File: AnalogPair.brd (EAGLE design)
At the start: 61 x 100.3 mm, 45 parts, among them J1 POWERPOLE_POWER25A, Q1 35A/25V/8.5mΩ, Q10 35A/25V/8.5mΩ, Q2 35A/25V/8.5mΩ, Q3 35A/25V/8.5mΩ, Q4 35A/25V/8.5mΩ, Q5 35A/25V/8.5mΩ, Q6 35A/25V/8.5mΩ, Q7 35A/25V/8.5mΩ, Q8 35A/25V/8.5mΩ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

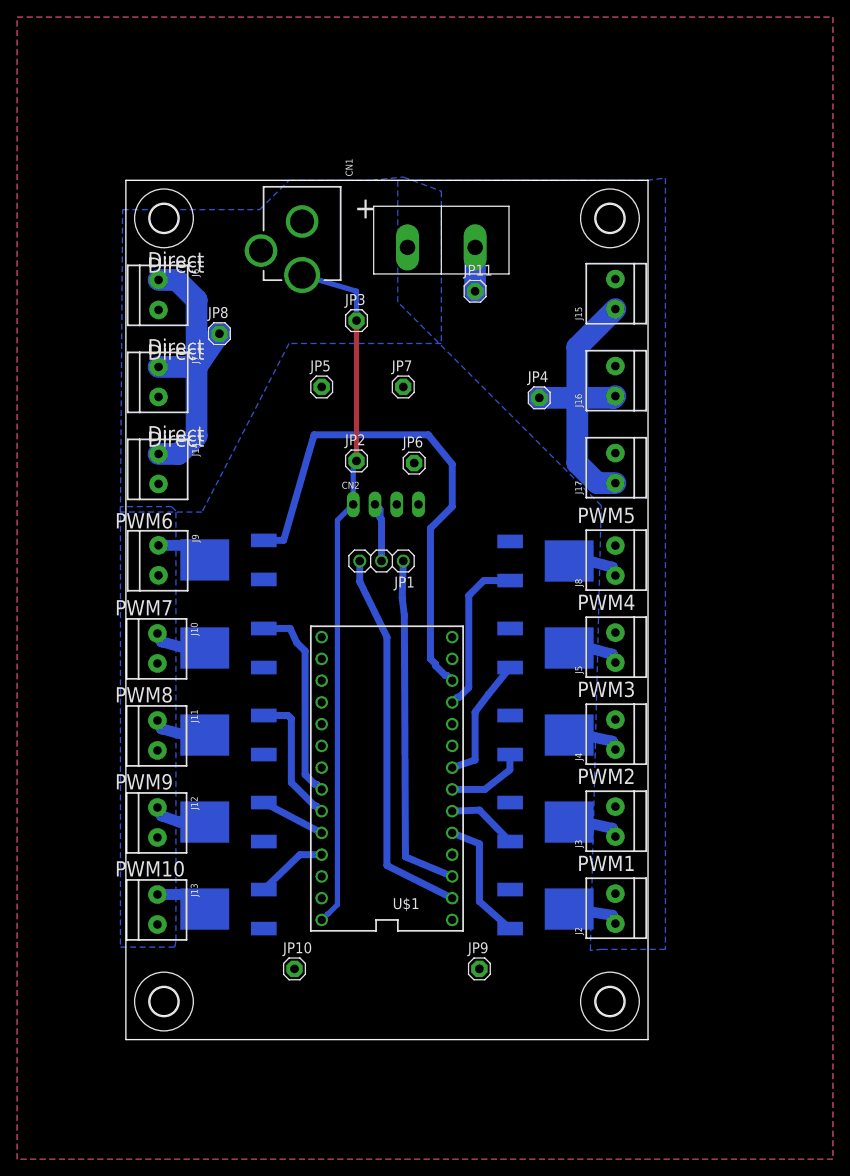
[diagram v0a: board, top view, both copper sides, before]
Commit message: added silks and submitted analogpair to allpcb.com
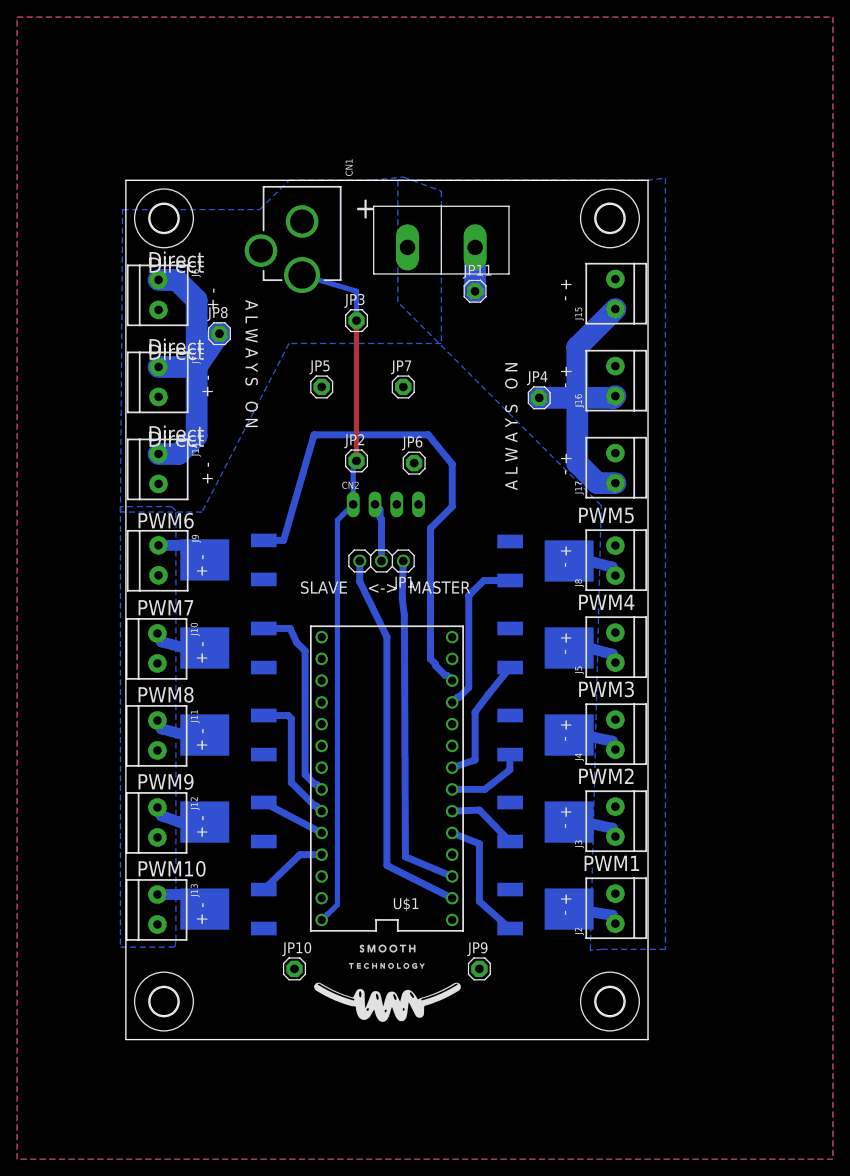
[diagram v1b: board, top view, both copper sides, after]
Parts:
- added U$13: (no value), SmoothTechnology:SMOOTH_
- added U$14: (no value), SmoothTechnology:TECHNOLOGY_
- added U$17: (no value), SmoothTechnology:SMOOTH_LOGO
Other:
- board text added: "+ -"
- board text added: "<->"
- board text added: "A L W A Y S O N"
- board text added: "MASTER"
- board text added: "SLAVE"
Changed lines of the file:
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@@
 <?xml version="1.0" encoding="utf-8"?>
 <!DOCTYPE eagle SYSTEM "eagle.dtd">
-<eagle version="8.5.2">
+<eagle version="8.6.0">
 <drawing>
 <settings>
-<setting alwaysvectorfont="no"/>
+<setting alwaysvectorfont="yes"/>
 <setting keepoldvectorfont="yes"/>
 <setting verticaltext="up"/>
@@
 <layer number="17" name="Pads" color="2" fill="1" visible="yes" active="yes"/>
 <layer number="18" name="Vias" color="2" fill="1" visible="yes" active="yes"/>
-<layer number="19" name="Unrouted" color="6" fill="1" visible="yes" active="yes"/>
-<layer number="20" name="Dimension" color="24" fill="1" visible="yes" active="yes"/>
+<layer number="19" name="Unrouted" color="6" fill="1" visible="no" active="yes"/>
+<layer number="20" name="Dimension" color="24" fill="1" visible="no" active="yes"/>
 <layer number="21" name="tPlace" color="7" fill="1" visible="yes" active="yes"/>
-<layer number="22" name="bPlace" color="7" fill="1" visible="yes" active="yes"/>
+<layer number="22" name="bPlace" color="7" fill="1" visible="no" active="yes"/>
 <layer number="23" name="tOrigins" color="15" fill="1" visible="yes" active="yes"/>
-<layer number="24" name="bOrigins" color="15" fill="1" visible="yes" active="yes"/>
-<layer number="25" name="tNames" color="7" fill="1" visible="yes" active="yes"/>
-<layer number="26" name="bNames" color="7" fill="1" visible="yes" active="yes"/>
-<layer number="27" name="tValues" color="7" fill="1" visible="yes" active="yes"/>
-<layer number="28" name="bValues" color="7" fill="1" visible="yes" active="yes"/>
+<layer number="24" name="bOrigins" color="15" fill="1" visible="no" active="yes"/>
+<layer number="25" name="tNames" color="7" fill="1" visible="no" active="yes"/>
+<layer number="26" name="bNames" color="7" fill="1" visible="no" active="yes"/>
+<layer number="27" name="tValues" color="7" fill="1" visible="no" active="yes"/>
+<layer number="28" name="bValues" color="7" fill="1" visible="no" active="yes"/>
 <layer number="29" name="tStop" color="7" fill="3" visible="no" active="yes"/>
 <layer number="30" name="bStop" color="7" fill="6" visible="no" active="yes"/>
@@
 <layer number="37" name="tTest" color="7" fill="1" visible="no" active="yes"/>
 <layer number="38" name="bTest" color="7" fill="1" visible="no" active="yes"/>
-<layer number="39" name="tKeepout" color="4" fill="11" visible="yes" active="yes"/>
-<layer number="40" name="bKeepout" color="1" fill="11" visible="yes" active="yes"/>
-<layer number="41" name="tRestrict" color="4" fill="10" visible="yes" active="yes"/>
-<layer number="42" name="bRestrict" color="1" fill="10" visible="yes" active="yes"/>
+<layer number="39" name="tKeepout" color="4" fill="11" visible="no" active="yes"/>
+<layer number="40" name="bKeepout" color="1" fill="11" visible="no" active="yes"/>
+<layer number="41" name="tRestrict" color="4" fill="10" visible="no" active="yes"/>
+<layer number="42" name="bRestrict" color="1" fill="10" visible="no" active="yes"/>
 <layer number="43" name="vRestrict" color="2" fill="10" visible="no" active="yes"/>
-<layer number="44" name="Drills" color="7" fill="1" visible="yes" active="yes"/>
-<layer number="45" name="Holes" color="7" fill="1" visible="yes" active="yes"/>
+<layer number="44" name="Drills" color="7" fill="1" visible="no" active="yes"/>
+<layer number="45" name="Holes" color="7" fill="1" visible="no" active="yes"/>
 <layer number="46" name="Milling" color="3" fill="1" visible="no" active="yes"/>
 <layer number="47" name="Measures" color="7" fill="1" visible="no" active="yes"/>
@@
 <layer number="49" name="Reference" color="7" fill="1" visible="no" active="yes"/>
 <layer number="50" name="dxf" color="7" fill="1" visible="no" active="no"/>
-<layer number="51" name="tDocu" color="7" fill="1" visible="yes" active="yes"/>
-<layer number="52" name="bDocu" color="7" fill="1" visible="yes" active="yes"/>
+<layer number="51" name="tDocu" color="7" fill="1" visible="no" active="yes"/>
+<layer number="52" name="bDocu" color="7" fill="1" visible="no" active="yes"/>
 <layer number="53" name="tGND_GNDA" color="7" fill="9" visible="no" active="no"/>
 <layer number="54" name="bGND_GNDA" color="1" fill="9" visible="no" active="no"/>
@@
 <text x="2.54" y="73.025" size="1.778" layer="25">Direct</text>
 <text x="2.54" y="62.865" size="1.778" layer="25">Direct</text>
-<text x="52.705" y="12.7" size="1.778" layer="21">PWM1</text>
+<text x="53.34" y="12.7" size="1.778" layer="21">PWM1</text>
 <text x="52.705" y="22.86" size="1.778" layer="21">PWM2</text>
 <text x="52.705" y="33.02" size="1.778" layer="21">PWM3</text>
 <text x="52.705" y="43.18" size="1.778" layer="21">PWM4</text>
 <text x="52.705" y="53.34" size="1.778" layer="21">PWM5</text>
-<text x="-1.27" y="52.705" size="1.778" layer="21">PWM6</text>
-<text x="-1.27" y="42.545" size="1.778" layer="21">PWM7</text>
-<text x="-1.27" y="32.385" size="1.778" layer="21">PWM8</text>
-<text x="-1.27" y="22.225" size="1.778" layer="21">PWM9</text>
-<text x="-1.27" y="12.065" size="1.778" layer="21">PWM10</text>
+<text x="1.27" y="52.705" size="1.778" layer="21">PWM6</text>
+<text x="1.27" y="42.545" size="1.778" layer="21">PWM7</text>
+<text x="1.27" y="32.385" size="1.778" layer="21">PWM8</text>
+<text x="1.27" y="22.225" size="1.778" layer="21">PWM9</text>
+<text x="1.27" y="12.065" size="1.778" layer="21">PWM10</text>
 <dimension x1="-2.54" y1="-6.985" x2="-2.54" y2="93.345" x3="-2.54" y3="43.18" textsize="1.778" layer="20" unit="inch"/>
+<text x="33.02" y="45.085" size="1.4224" layer="21">MASTER</text>
+<text x="20.32" y="45.085" size="1.4224" layer="21">SLAVE</text>
+<text x="28.194" y="45.085" size="1.4224" layer="21">&lt;-&gt;</text>
+<text x="9.525" y="6.35" size="1.4224" layer="21" ratio="15" rot="R90">+ -</text>
+<text x="9.525" y="16.51" size="1.4224" layer="21" ratio="15" rot="R90">+ -</text>
+<text x="9.525" y="26.67" size="1.4224" layer="21" ratio="15" rot="R90">+ -</text>
+<text x="9.525" y="36.83" size="1.4224" layer="21" ratio="15" rot="R90">+ -</text>
+<text x="9.525" y="46.99" size="1.4224" layer="21" ratio="15" rot="R90">+ -</text>
+<text x="10.16" y="57.785" size="1.4224" layer="21" ratio="15" rot="R90">+ -</text>
+<text x="10.16" y="67.945" size="1.4224" layer="21" ratio="15" rot="R90">+ -</text>
+<text x="10.795" y="78.105" size="1.4224" layer="21" ratio="15" rot="R90">+ -</text>
+<text x="50.8" y="81.915" size="1.4224" layer="21" ratio="15" rot="SR270">+ -</text>
+<text x="50.8" y="71.755" size="1.4224" layer="21" ratio="15" rot="SR270">+ -</text>
+<text x="50.8" y="61.595" size="1.4224" layer="21" ratio="15" rot="SR270">+ -</text>
+<text x="50.8" y="50.8" size="1.4224" layer="21" ratio="15" rot="SR270">+ -</text>
+<text x="50.8" y="40.64" size="1.4224" layer="21" ratio="15" rot="SR270">+ -</text>
+<text x="50.8" y="30.48" size="1.4224" layer="21" ratio="15" rot="SR270">+ -</text>
+<text x="50.8" y="20.32" size="1.4224" layer="21" ratio="15" rot="SR270">+ -</text>
+<text x="50.8" y="10.16" size="1.4224" layer="21" ratio="15" rot="SR270">+ -</text>
+<text x="45.72" y="57.15" size="1.4224" layer="21" ratio="10" rot="R90">A L W A Y S   O N</text>
+<text x="13.97" y="79.375" size="1.4224" layer="21" ratio="10" rot="SR270">A L W A Y S   O N</text>
 </plain>
 <attributes>
@@
 <element name="JP10" library="adafruit" package="1X01" value="" x="19.685" y="1.27"/>
 <element name="JP11" library="adafruit" package="1X01" value="" x="40.767" y="80.391"/>
+<element name="U$13" library="SmoothTechnology" package="SMOOTH_" value="" x="27.305" y="3.175"/>
+<element name="U$14" library="SmoothTechnology" package="TECHNOLOGY_" value="" x="26.035" y="1.27"/>
+<element name="U$17" library="SmoothTechnology" package="SMOOTH_LOGO" value="" x="30.48" y="-3.175"/>
 </elements>
 <signals>
